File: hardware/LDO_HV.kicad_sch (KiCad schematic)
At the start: 5 parts, among them U1 MCP1826S

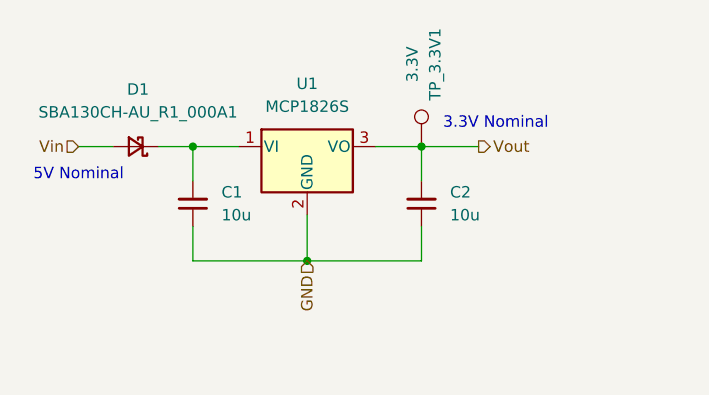
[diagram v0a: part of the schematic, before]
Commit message: labeled + stm32 cube layout
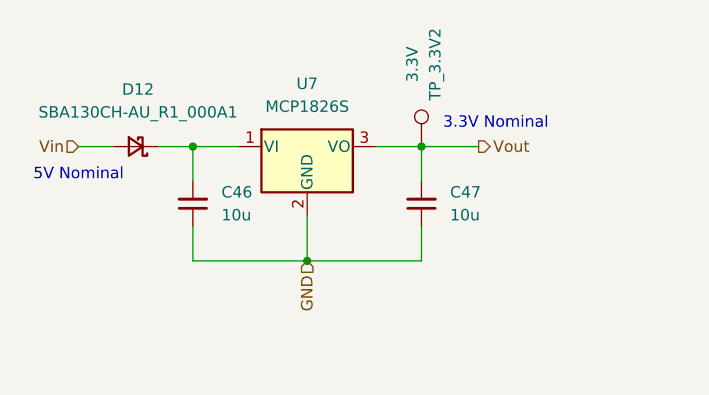
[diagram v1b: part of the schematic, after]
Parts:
- renumbered C1 to C46, C2 to C47, D1 to D12, TP_3.3V1 to TP_3.3V2, U1 to U7
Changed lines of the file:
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@@
 		(dnp no)
 		(fields_autoplaced yes)
-		(property "Reference" "C2"
+		(property "Reference" "C47"
 			(at 168.275 68.5735 0)
 			(effects
@@
 			(project "LDO"
 				(path "/2365a867-6254-4a7c-9718-f325e0bbac5c/904fa10a-747c-46cf-90d1-33d76069dc5d/65331a51-ccf3-4481-a1ca-d2dd52d3f2f0"
-					(reference "C2")
+					(reference "C47")
 					(unit 1)
 				)
@@
 		(on_board yes)
 		(dnp no)
-		(property "Reference" "TP_3.3V1"
+		(property "Reference" "TP_3.3V2"
 			(at 166.624 54.356 90)
 			(effects
@@
 			(project "LDO"
 				(path "/2365a867-6254-4a7c-9718-f325e0bbac5c/904fa10a-747c-46cf-90d1-33d76069dc5d/65331a51-ccf3-4481-a1ca-d2dd52d3f2f0"
-					(reference "TP_3.3V1")
+					(reference "TP_3.3V2")
 					(unit 1)
 				)
@@
 		(dnp no)
 		(fields_autoplaced yes)
-		(property "Reference" "U1"
+		(property "Reference" "U7"
 			(at 152.4 56.515 0)
 			(effects
@@
 			(project ""
 				(path "/2365a867-6254-4a7c-9718-f325e0bbac5c/904fa10a-747c-46cf-90d1-33d76069dc5d/65331a51-ccf3-4481-a1ca-d2dd52d3f2f0"
-					(reference "U1")
+					(reference "U7")
 					(unit 1)
 				)
@@
 		(dnp no)
 		(fields_autoplaced yes)
-		(property "Reference" "D1"
+		(property "Reference" "D12"
 			(at 133.604 57.15 0)
 			(effects
@@
 			(project ""
 				(path "/2365a867-6254-4a7c-9718-f325e0bbac5c/904fa10a-747c-46cf-90d1-33d76069dc5d/65331a51-ccf3-4481-a1ca-d2dd52d3f2f0"
-					(reference "D1")
+					(reference "D12")
 					(unit 1)
 				)
@@
 		(dnp no)
 		(fields_autoplaced yes)
-		(property "Reference" "C1"
+		(property "Reference" "C46"
 			(at 142.875 68.5735 0)
 			(effects
@@
 			(project "LDO"
 				(path "/2365a867-6254-4a7c-9718-f325e0bbac5c/904fa10a-747c-46cf-90d1-33d76069dc5d/65331a51-ccf3-4481-a1ca-d2dd52d3f2f0"
-					(reference "C1")
-					(unit 1)
-				)
+					(reference "C46")
+					(unit 1)
+				)

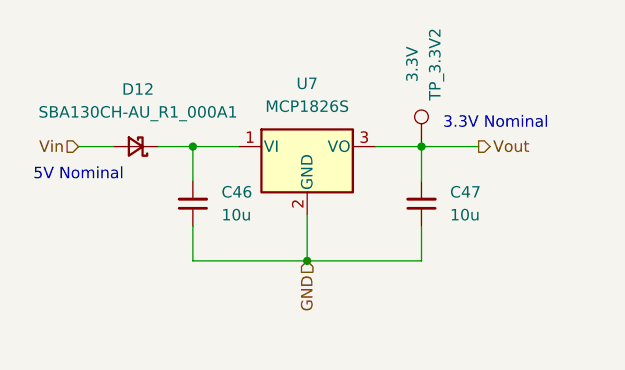
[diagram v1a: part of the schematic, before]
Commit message: added debug led
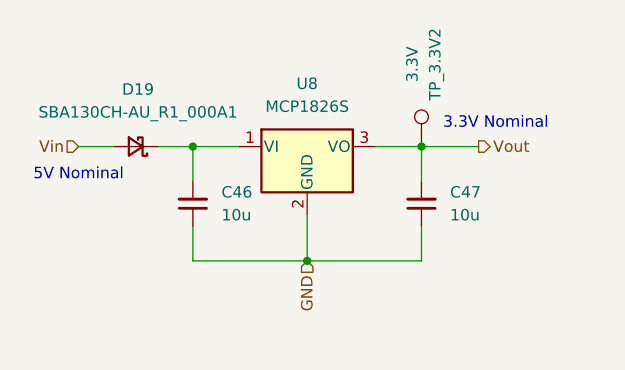
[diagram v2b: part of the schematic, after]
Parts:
- renumbered D12 to D19, U7 to U8
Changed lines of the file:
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@@
 		(dnp no)
 		(fields_autoplaced yes)
-		(property "Reference" "U7"
+		(property "Reference" "U8"
 			(at 152.4 56.515 0)
 			(effects
@@
 			(project ""
 				(path "/2365a867-6254-4a7c-9718-f325e0bbac5c/904fa10a-747c-46cf-90d1-33d76069dc5d/65331a51-ccf3-4481-a1ca-d2dd52d3f2f0"
-					(reference "U7")
+					(reference "U8")
 					(unit 1)
 				)
@@
 		(dnp no)
 		(fields_autoplaced yes)
-		(property "Reference" "D12"
+		(property "Reference" "D19"
 			(at 133.604 57.15 0)
 			(effects
@@
 			(project ""
 				(path "/2365a867-6254-4a7c-9718-f325e0bbac5c/904fa10a-747c-46cf-90d1-33d76069dc5d/65331a51-ccf3-4481-a1ca-d2dd52d3f2f0"
-					(reference "D12")
+					(reference "D19")
 					(unit 1)
 				)
